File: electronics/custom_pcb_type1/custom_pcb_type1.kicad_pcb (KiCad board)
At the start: 2 copper layers, 25 parts, among them J1 BELT_CONN_1, J2 BELT_CONN_2, J3 SEN0140, J4 USB_B, Q1 2N2222, Q2 2N2222, Q3 2N2222, Q4 2N2222, Q5 2N2222, Q6 2N2222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

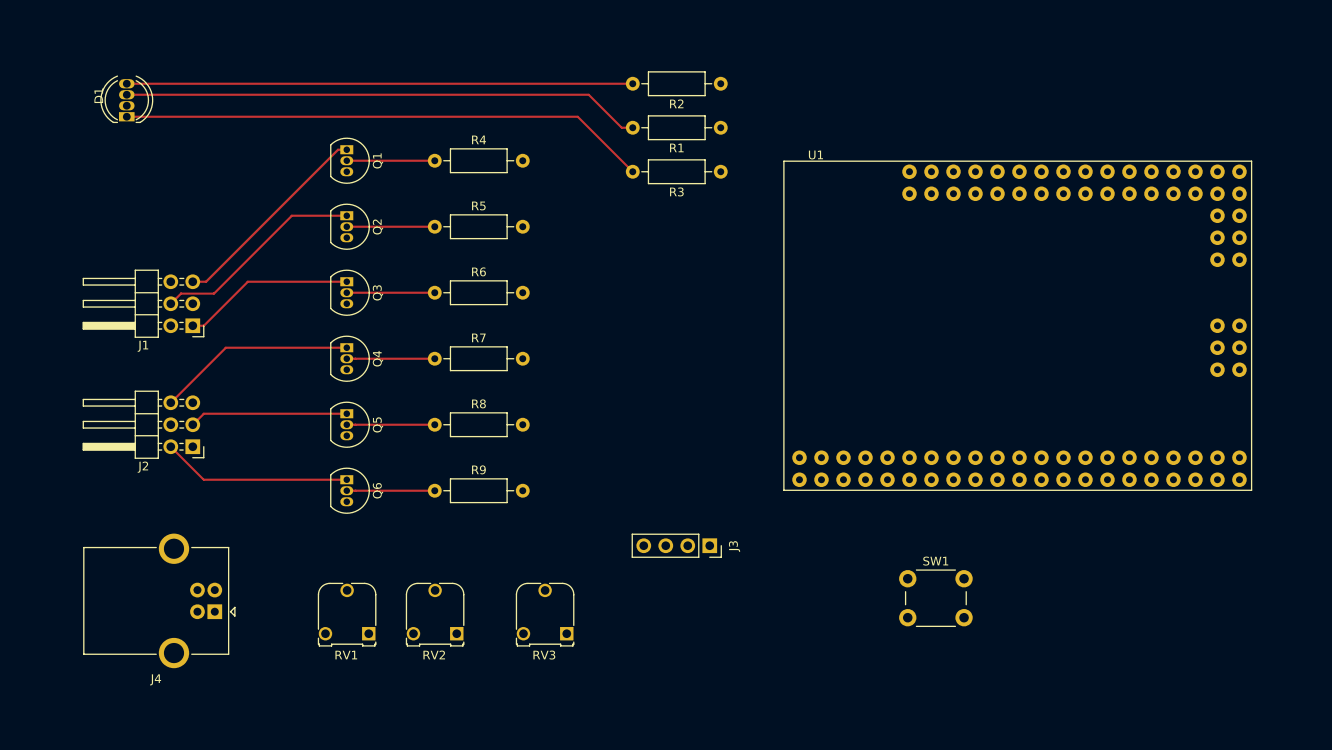
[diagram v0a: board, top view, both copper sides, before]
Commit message: Better PCB routing
Before I started doing the back side routing I decided to try rerouting things for more traces on the top layer. I ended up changing the pinout to use even numbered pins 2-12 backwards (i.e. first motor is on pin 12, last motor on pin 2). That made routing SO much easier and I probably should have done that first. Now I think I'm down to just power and ground traces which I will have to do on the back for the most part. I know generally you're supposed to put data and power on the top layer and ground traces on the bottom but in this case just finishing it is all I want. Our bottom layer will be carefully placed ground and power traces unless we can finagle more room out of the top.
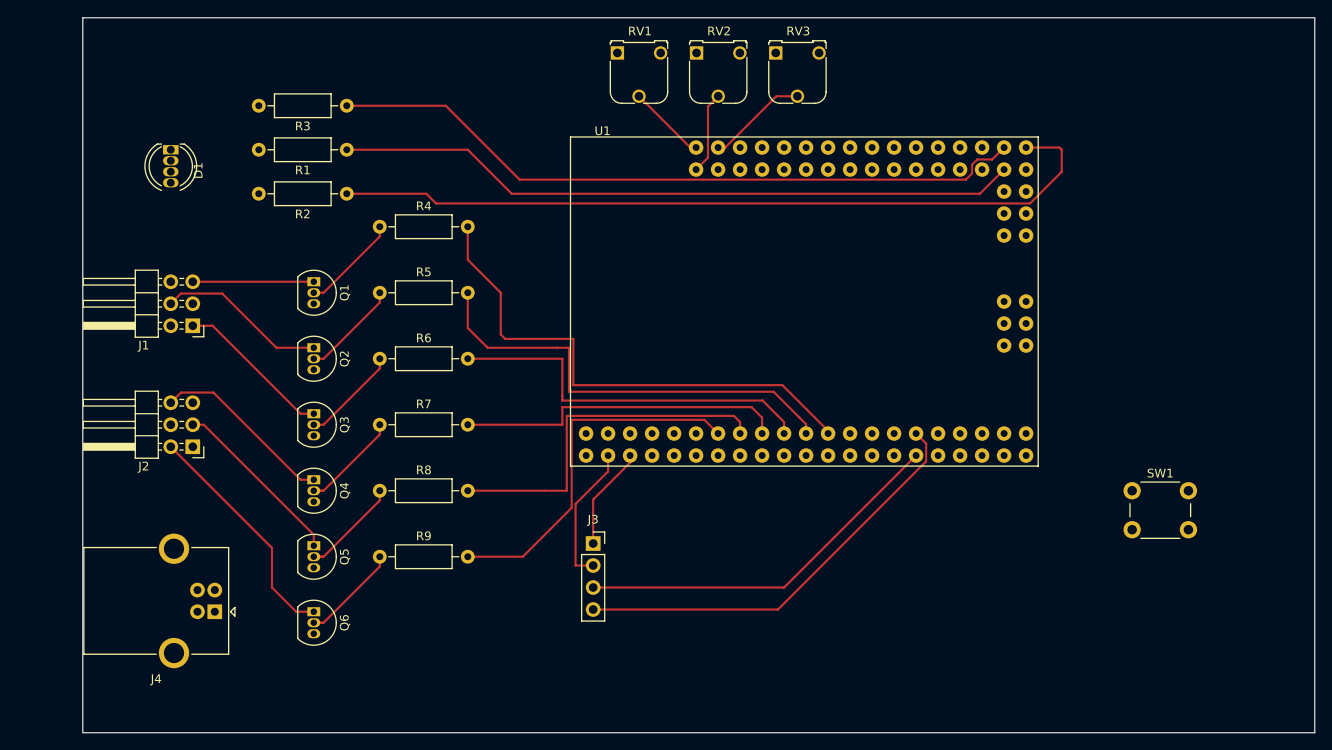
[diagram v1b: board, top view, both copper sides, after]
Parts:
- moved RV1 72.9 mm to (129.0, 70.1), turned to 0 degrees
- moved RV2 72.5 mm to (138.2, 70.1), turned to 0 degrees
- moved RV3 71.3 mm to (147.3, 70.1), turned to 0 degrees
- moved R2 45.0 mm to (97.8, 86.4)
- moved R3 43.8 mm to (97.8, 76.2)
- moved R1 43.3 mm to (97.8, 81.3)
- moved SW1 27.8 mm to (188.5, 120.7)
- moved U1 24.8 mm to (150.6, 98.8)
- moved Q3 15.7 mm to (94.0, 111.8)
- moved Q6 15.7 mm to (94.0, 134.6)
- moved Q1 15.7 mm to (94.0, 96.5)
- moved Q2 15.7 mm to (94.0, 104.1)
- moved Q4 15.7 mm to (94.0, 119.4)
- moved Q5 15.7 mm to (94.0, 127.0)
- moved J3 13.5 mm to (126.2, 126.7), turned to 0 degrees
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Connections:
- J3 pad 1: +5V -> Net-(J3-Pad1)
- J3 pad 2: GND -> Net-(J3-Pad2)
- SW1 pad 1: Net-(SW1-Pad1) -> GND
- SW1 pad 2: Net-(SW1-Pad1) -> Net-(SW1-Pad2)
- U1 pad 5V_1: +5V -> Net-(J3-Pad1)
- U1 pad 5V_2: Net-(U1-Pad5V_1) -> Net-(J3-Pad1)
- U1 pad 5V_3: Net-(U1-Pad5V_1) -> Net-(J3-Pad1)
- U1 pad D10: Net-(R9-Pad2) -> Net-(R5-Pad2)
- U1 pad D12: Net-(U1-PadD12) -> Net-(R4-Pad2)
- U1 pad D2: Net-(U1-PadD2) -> Net-(R9-Pad2)
- U1 pad D4: Net-(U1-PadD4) -> Net-(R8-Pad2)
- U1 pad D5: Net-(R4-Pad2) -> Net-(U1-PadD5)
- U1 pad D6: Net-(R5-Pad2) -> Net-(R7-Pad2)
- U1 pad D7: Net-(R6-Pad2) -> Net-(U1-PadD7)
- U1 pad D8: Net-(R7-Pad2) -> Net-(R6-Pad2)
- U1 pad D9: Net-(R8-Pad2) -> Net-(U1-PadD9)
- U1 pad GND_1: GND -> Net-(J3-Pad2)
- U1 pad GND_2: GND -> Net-(J3-Pad2)
- U1 pad GND_3: Net-(U1-PadGND_1) -> Net-(J3-Pad2)
- U1 pad RST: Net-(SW1-Pad1) -> Net-(SW1-Pad2)
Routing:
- net Net-(R2-Pad1): track 0.00 -> 91.3 mm
- net Net-(R3-Pad1): track 0.00 -> 81.6 mm
- net Net-(R1-Pad1): track 0.00 -> 79.2 mm
- net Net-(D1-Pad1): track 61.1 -> 0.00 mm
- net Net-(D1-Pad3): track 60.0 -> 0.00 mm
- net Net-(R4-Pad2): track 0.00 -> 59.9 mm
- net Net-(D1-Pad4): track 58.4 -> 0.00 mm
- net Net-(R5-Pad2): track 0.00 -> 52.0 mm
- net Net-(J3-Pad4): track 0.00 -> 49.2 mm
- net Net-(R6-Pad2): track 0.00 -> 43.9 mm
- net Net-(J3-Pad3): track 0.00 -> 43.6 mm
- net Net-(R9-Pad2): track 0.00 -> 42.1 mm
- net Net-(R8-Pad2): track 0.00 -> 41.7 mm
- net Net-(R7-Pad2): track 0.00 -> 38.3 mm
- net Net-(J3-Pad2): track 0.00 -> 16.3 mm
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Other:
- board outline added: 142.2 x 82.5 mm

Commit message: PCB version 1.0
Ok I've finished laying everything out. In the end I was successful in laying out the data and power traces on top and only have ground traces on the bottom. I've generated the reversed masks that are ready for laser printing. Now I'm realizing that transferring the mask to the PCB is going to be a slightly involved task. I've settled on the rolling pin + hotplate method since I don't want to build a jig to hold an iron upside down and I don't want to spend the time modifying a cheap ebay laminator to work with PCBs. Going forward I may switch to a photoetching process instead since that doesn't require heat+pressure. Although it requires a few more chemicals it seems like a more controllable process. I did price out an online mfg and it was around $50 shipped for 5 boards. I'd be amazed if the first version of this board actually even works but maybe a future version I will order online instead.

Also something happened with the symbol library for the project and it generated a rescue lib. No idea why but it seems fine.
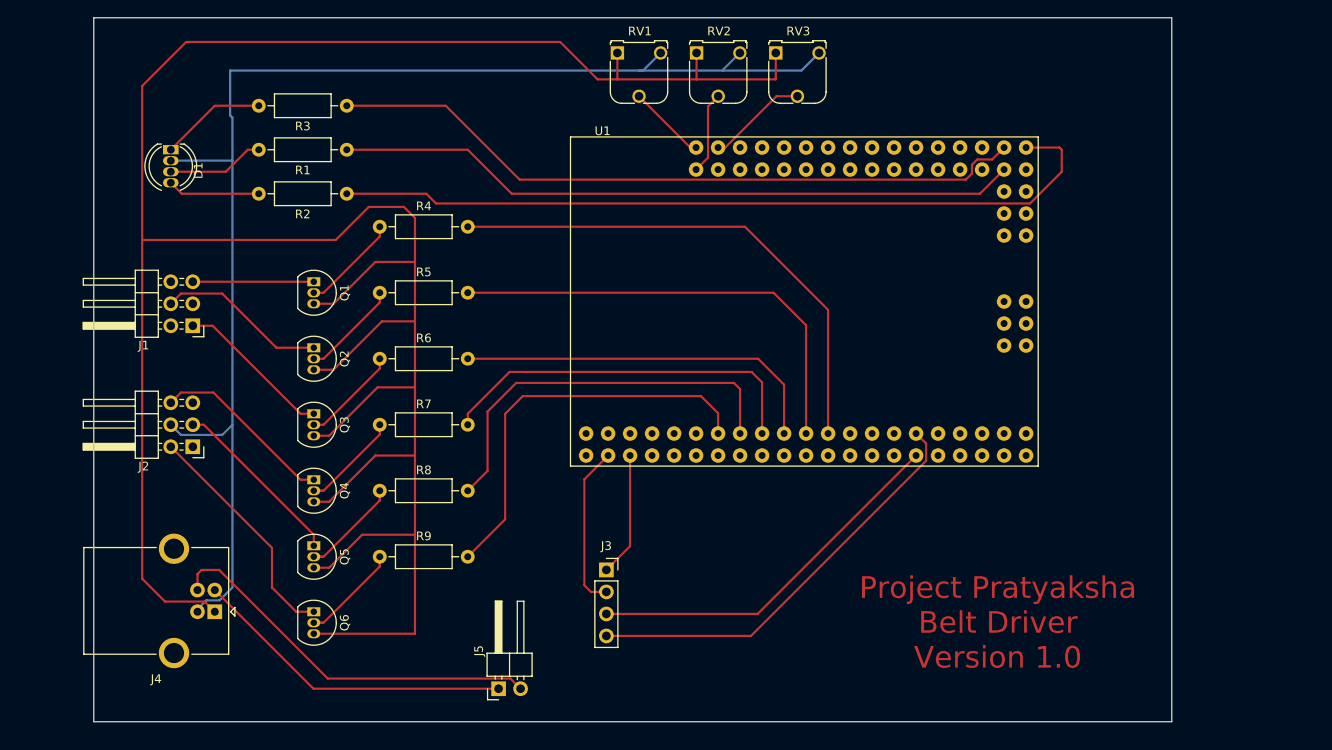
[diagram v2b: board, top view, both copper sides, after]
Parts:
- removed SW1: RST_SW, Button_Switch_THT:SW_PUSH_6mm
- added J5: JMPR_TO_ATMEGA, Connector_PinHeader_2.54mm:PinHeader_1x02_P2.54mm_Horizontal, F.Cu at (115.3, 143.5)
- moved J3 3.41 mm to (127.8, 129.8)
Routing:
- net +5V: track 0.00 -> 315.2 mm
- net GND: track 0.00 -> 155.3 mm
- net Net-(J4-Pad3): track 0.00 -> 45.0 mm
- net Net-(J4-Pad2): track 0.00 -> 37.5 mm
- net Net-(D1-Pad1): track 0.00 -> 12.3 mm
- net Net-(D1-Pad3): track 0.00 -> 11.2 mm
- net Net-(D1-Pad4): track 0.00 -> 10.7 mm
- net Net-(R7-Pad2): track 38.3 -> 43.7 mm
- net Net-(R9-Pad2): track 42.1 -> 46.9 mm
- net Net-(R8-Pad2): track 41.7 -> 46.0 mm
- net Net-(J3-Pad1): track 11.9 -> 15.2 mm
- net Net-(J3-Pad2): track 16.3 -> 19.0 mm
- net Net-(R5-Pad2): track 52.0 -> 53.1 mm
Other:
- board size 142.2 x 82.5 mm -> 124.5 x 81.3 mm
- rule trace_min: 0.2 -> 0.6
- board text added: "Project Pratyaksha Belt Driver Version 1.0"

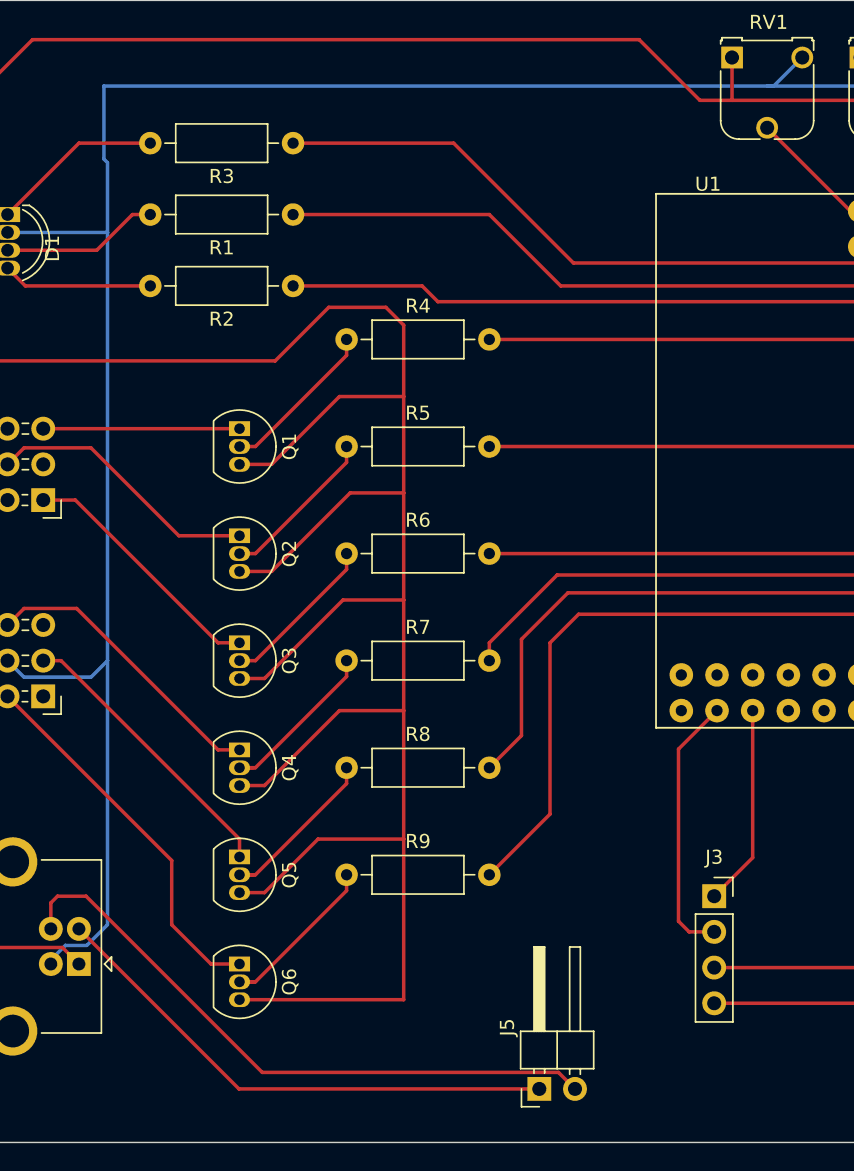
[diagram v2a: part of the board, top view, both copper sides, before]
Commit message: Cleaned up traces
Looking at the mask I saw a couple spots where It was questionable if it would etch properly. I just separated out the traces the best I could. I'm wondering if I could remove the unused pins of the atmega from its footprint so I can route traces there instead. Currently all the unused pins are still masked and will be etched around, leaving behind copper pads that will later be drilled out.
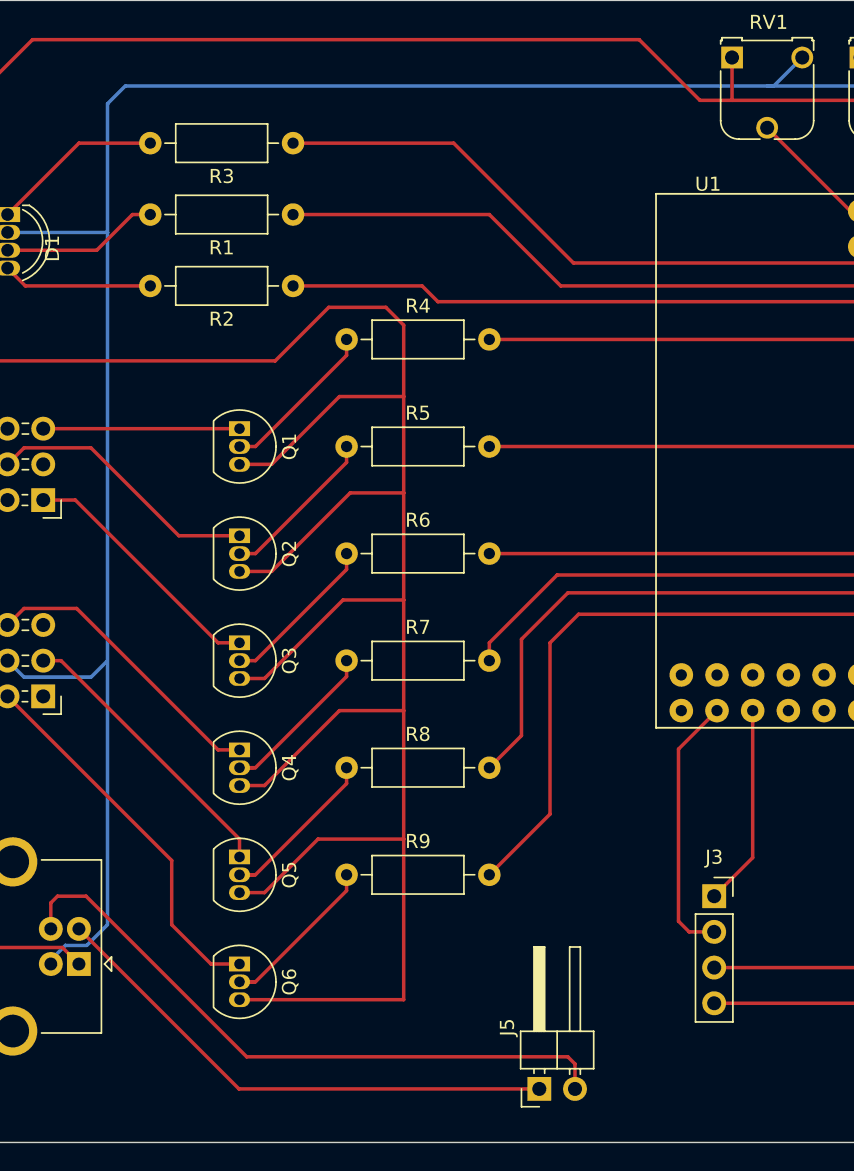
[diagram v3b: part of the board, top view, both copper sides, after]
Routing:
- net GND: track 155.3 -> 154.2 mm
- net Net-(J4-Pad3): track 45.0 -> 46.1 mm
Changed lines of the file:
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@@
   (page A4)
   (layers
-    (0 F.Cu signal)
+    (0 F.Cu signal hide)
     (31 B.Cu signal)
     (33 F.Adhes user)
@@
     (visible_elements 7FFFFFFF)
     (pcbplotparams
-      (layerselection 0x010fc_ffffffff)
+      (layerselection 0x00000_ffffffff)
       (usegerberextensions false)
       (usegerberattributes true)
       (usegerberadvancedattributes true)
       (creategerberjobfile true)
-      (excludeedgelayer true)
+      (excludeedgelayer false)
       (linewidth 0.100000)
       (plotframeref false)
@@
       (padsonsilk false)
       (subtractmaskfromsilk false)
-      (outputformat 1)
-      (mirror false)
+      (outputformat 4)
+      (mirror true)
       (drillshape 1)
       (scaleselection 1)
-      (outputdirectory ""))
+      (outputdirectory "C:/Users/Kyle/Documents/GitHub/project_pratyaksha/electronics/custom_pcb_type1/masks/version_1.0"))
   )
   (net 0 "")
@@
   (segment (start 80.55 134.334998) (end 81.589997 133.295001) (width 0.25) (layer B.Cu) (net 3) (status 10))
   (segment (start 80.55 134.62) (end 80.55 134.334998) (width 0.25) (layer B.Cu) (net 3) (status 30))
-  (segment (start 84.582 77.582998) (end 84.328 77.328998) (width 0.25) (layer B.Cu) (net 3))
-  (segment (start 84.328 77.328998) (end 84.328 72.136) (width 0.25) (layer B.Cu) (net 3))
   (segment (start 150.288 72.136) (end 152.32 70.104) (width 0.25) (layer B.Cu) (net 3) (status 20))
   (segment (start 141.224 72.056) (end 141.224 72.136) (width 0.25) (layer B.Cu) (net 3))
@@
   (segment (start 134.032 70.104) (end 132 72.136) (width 0.25) (layer B.Cu) (net 3) (status 10))
   (segment (start 131.572 72.136) (end 141.224 72.136) (width 0.25) (layer B.Cu) (net 3))
-  (segment (start 84.328 72.136) (end 131.572 72.136) (width 0.25) (layer B.Cu) (net 3))
   (segment (start 83.406999 114.205001) (end 84.582 113.03) (width 0.25) (layer B.Cu) (net 3))
   (segment (start 78.645001 114.205001) (end 83.406999 114.205001) (width 0.25) (layer B.Cu) (net 3))
@@
   (segment (start 84.582 131.827002) (end 84.582 113.03) (width 0.25) (layer B.Cu) (net 3))
   (segment (start 77.47 82.55) (end 84.582 82.55) (width 0.25) (layer B.Cu) (net 3) (status 10))
-  (segment (start 84.582 82.55) (end 84.582 77.582998) (width 0.25) (layer B.Cu) (net 3))
   (segment (start 84.582 113.03) (end 84.582 82.55) (width 0.25) (layer B.Cu) (net 3))
+  (segment (start 85.852 72.136) (end 131.572 72.136) (width 0.25) (layer B.Cu) (net 3))
+  (segment (start 84.582 73.406) (end 85.852 72.136) (width 0.25) (layer B.Cu) (net 3))
+  (segment (start 84.582 82.55) (end 84.582 73.406) (width 0.25) (layer B.Cu) (net 3))
   (segment (start 93.98 111.76) (end 92.456 111.76) (width 0.25) (layer F.Cu) (net 5) (status 10))
   (segment (start 92.456 111.76) (end 82.296 101.6) (width 0.25) (layer F.Cu) (net 5))
@@
   (segment (start 138.176 73.152) (end 129.032 73.152) (width 0.25) (layer F.Cu) (net 17))
   (segment (start 147.32 73.152) (end 138.176 73.152) (width 0.25) (layer F.Cu) (net 17))
-  (segment (start 116.680999 142.334999) (end 95.598999 142.334999) (width 0.25) (layer F.Cu) (net 19))
-  (segment (start 117.856 143.51) (end 116.680999 142.334999) (width 0.25) (layer F.Cu) (net 19))
-  (segment (start 95.598999 142.334999) (end 83.058 129.794) (width 0.25) (layer F.Cu) (net 19))
   (segment (start 83.058 129.794) (end 81.026 129.794) (width 0.25) (layer F.Cu) (net 19))
   (segment (start 80.55 130.27) (end 81.026 129.794) (width 0.25) (layer F.Cu) (net 19))
   (segment (start 80.55 132.12) (end 80.55 130.27) (width 0.25) (layer F.Cu) (net 19))
+  (segment (start 117.856 143.51) (end 117.856 141.732) (width 0.25) (layer F.Cu) (net 19))
+  (segment (start 117.856 141.732) (end 117.348 141.224) (width 0.25) (layer F.Cu) (net 19))
+  (segment (start 94.488 141.224) (end 83.058 129.794) (width 0.25) (layer F.Cu) (net 19))
+  (segment (start 117.348 141.224) (end 94.488 141.224) (width 0.25) (layer F.Cu) (net 19))
   (segment (start 93.94 143.51) (end 115.316 143.51) (width 0.25) (layer F.Cu) (net 20))
   (segment (start 82.55 132.12) (end 93.94 143.51) (width 0.25) (layer F.Cu) (net 20))
